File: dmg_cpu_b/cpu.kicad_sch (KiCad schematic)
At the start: 1 part

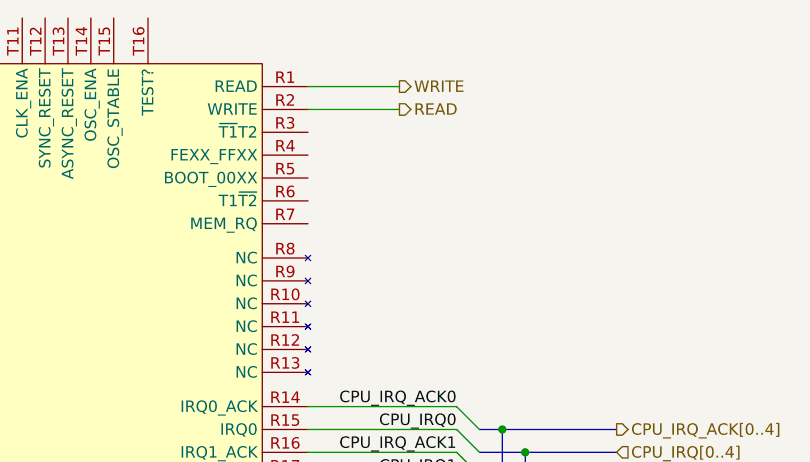
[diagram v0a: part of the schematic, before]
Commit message: addr and data buses added and split on 2 sheets.
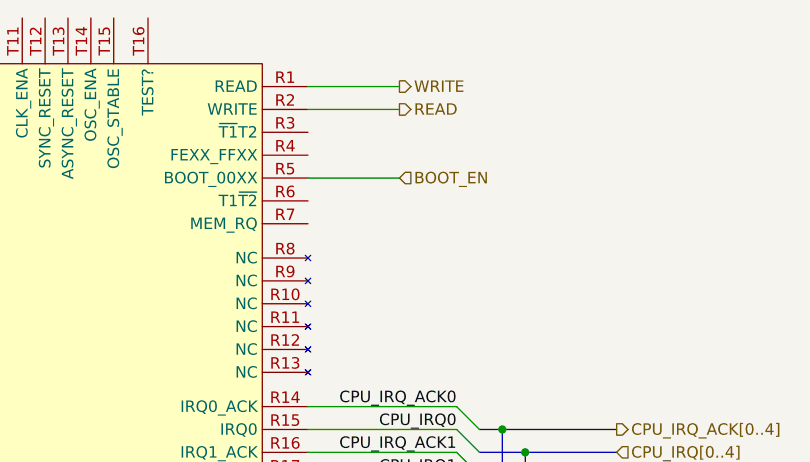
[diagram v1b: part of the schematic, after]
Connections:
- net BOOT_EN: now reaches U?.R5 (BOOT_00XX)
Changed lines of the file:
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@@
+    (stroke (width 0) (type default) (color 0 0 0 0))
+  )
+  (wire (pts (xy 184.15 64.77) (xy 173.99 64.77))
     (stroke (width 0) (type default) (color 0 0 0 0))
   )
@@
     (effects (font (size 1.27 1.27)) (justify right bottom))
   )
+  (hierarchical_label "BOOT_EN" (shape input) (at 184.15 64.77 0)
+    (effects (font (size 1.27 1.27)) (justify left))
+  )
   (hierarchical_label "CPU_IRQ[0..4]" (shape output) (at 363.855 252.73 0)

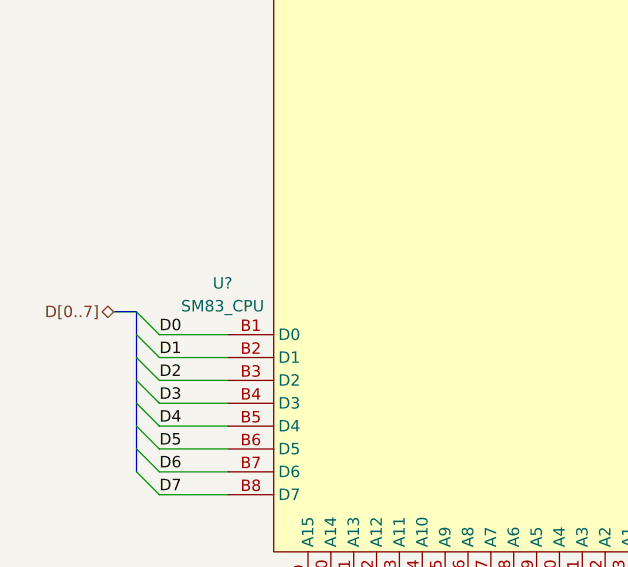
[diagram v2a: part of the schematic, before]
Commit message: fixes made following review
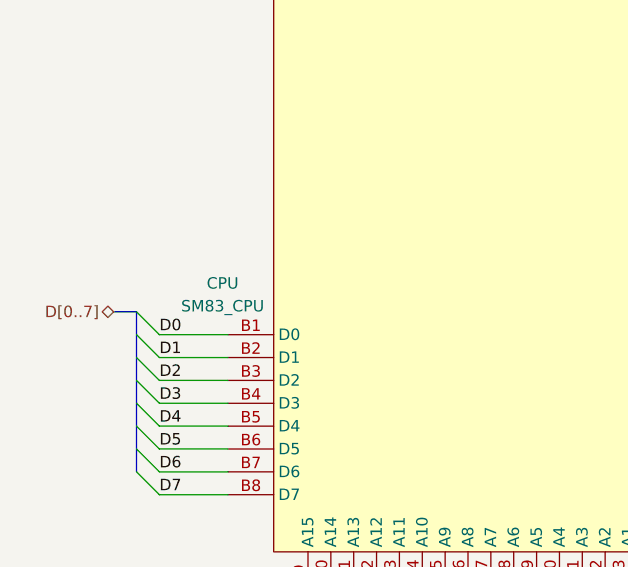
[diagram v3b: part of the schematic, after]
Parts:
- gave numbers to parts that had none: 1
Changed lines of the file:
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@@
   (symbol (lib_id "DMG_CPU_Cells:SM83_CPU") (at 139.7 91.44 0) (unit 1)
     (in_bom yes) (on_board yes) (fields_autoplaced)
-    (property "Reference" "U?" (id 0) (at 104.8166 100.9735 0))
+    (property "Reference" "CPU" (id 0) (at 104.8166 100.9735 0))
     (property "Value" "SM83_CPU" (id 1) (at 104.8166 103.5104 0))
     (property "Footprint" "" (id 2) (at 143.51 91.44 0)

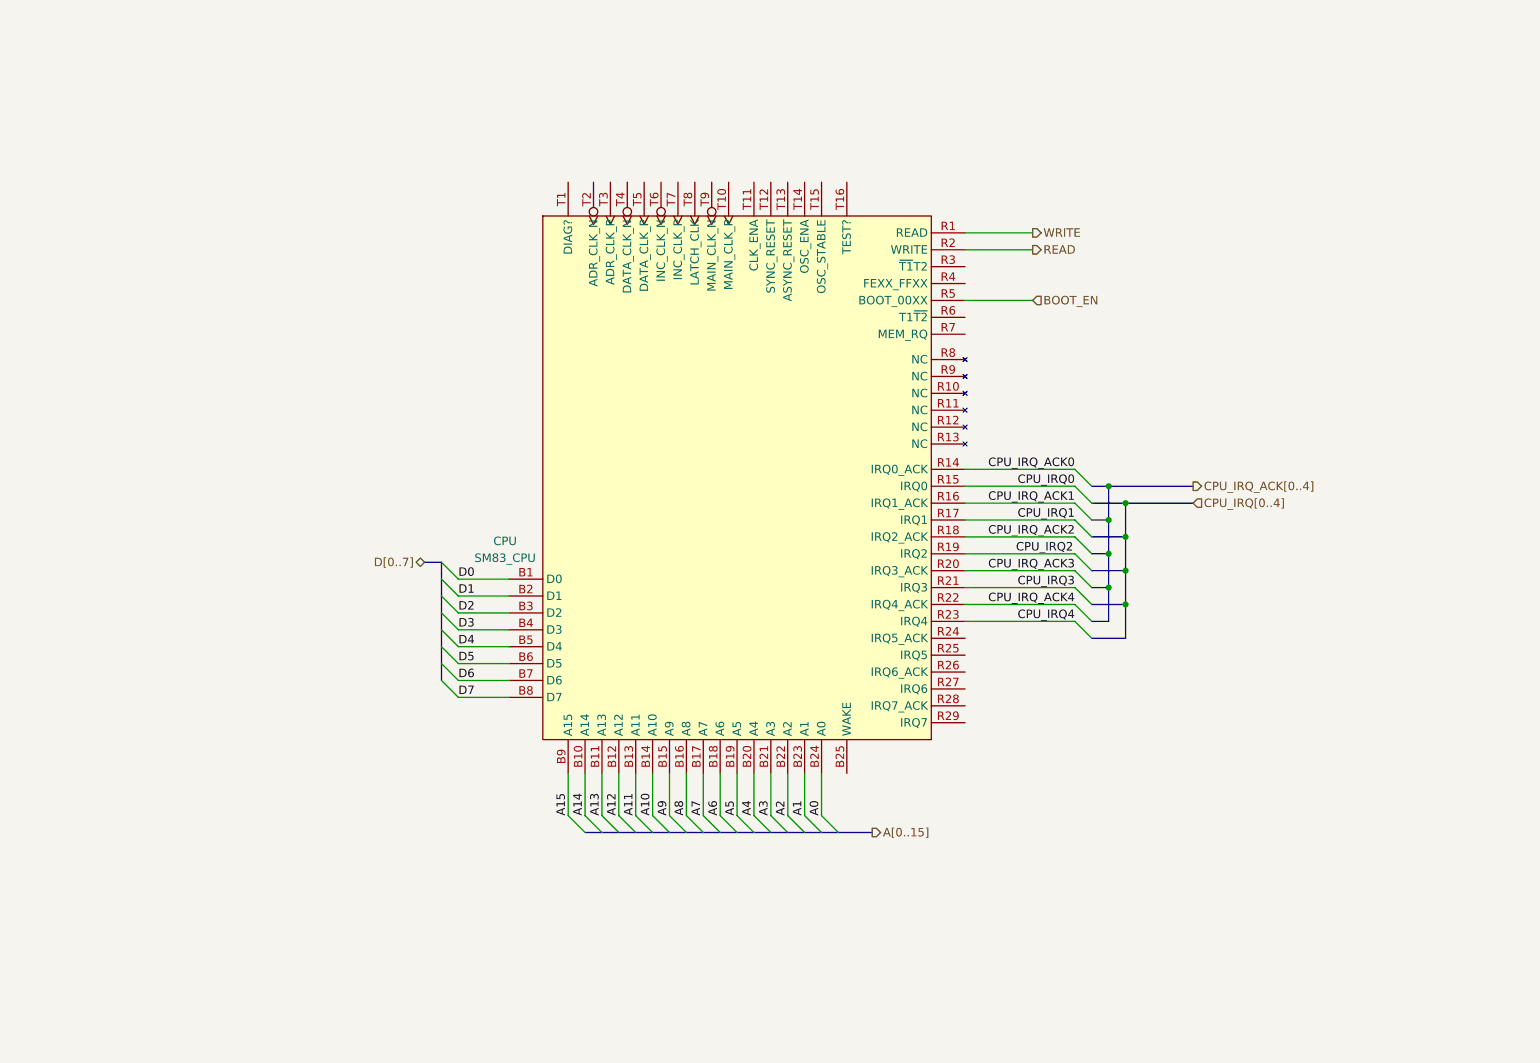
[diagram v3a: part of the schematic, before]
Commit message: VRAM interface sheet added but various edits in existing sheets. Notable merge of RESET, CLOCKS and FF04 DIV sheets
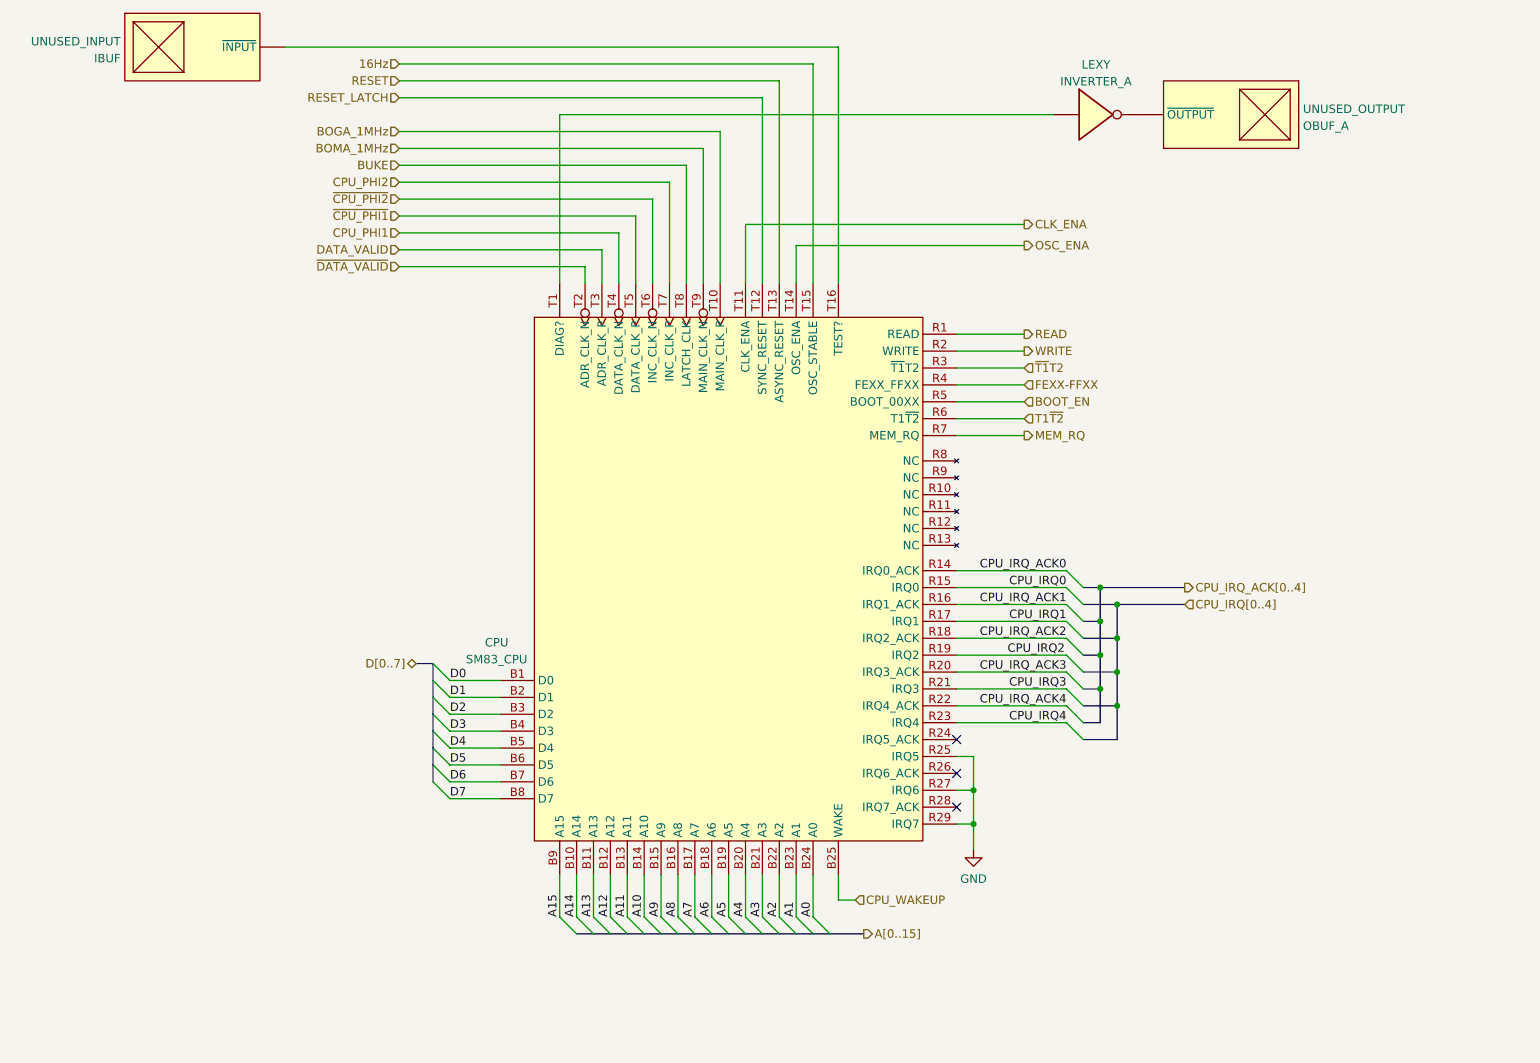
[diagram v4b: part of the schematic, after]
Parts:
- added LEXY: INVERTER_A, symbol DMG_CPU_Cells:INVERTER_A
- added UNUSED_INPUT: IBUF, symbol DMG_CPU_Cells:IBUF
- added UNUSED_OUTPUT: OBUF_A, symbol DMG_CPU_Cells:OBUF_A
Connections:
- net READ: now also CPU.R1 (READ); no longer CPU.R2 (WRITE)
- net WRITE: now also CPU.R2 (WRITE); no longer CPU.R1 (READ)
- net CPU_WAKEUP: now reaches CPU.B25 (WAKE)
- net GND: now reaches CPU.R25 (IRQ5)
- net GND: now also CPU.R27 (IRQ6), CPU.R29 (IRQ7)
- net ~{T1}T2: now reaches CPU.R3 (~{T1}T2)
- net FEXX-FFXX: now reaches CPU.R4 (FEXX_FFXX)
- net T1~{T2}: now reaches CPU.R6 (T1~{T2})
- net MEM_RQ: now reaches CPU.R7 (MEM_RQ)
- net at CPU.T1 (DIAG?): now also LEXY.1
- net BOGA_1MHz: now reaches CPU.T10 (MAIN_CLK_P)
- net CLK_ENA: now reaches CPU.T11 (CLK_ENA)
- net RESET_LATCH: now reaches CPU.T12 (SYNC_RESET)
- net RESET: now reaches CPU.T13 (ASYNC_RESET)
- net OSC_ENA: now reaches CPU.T14 (OSC_ENA)
- net 16Hz: now reaches CPU.T15 (OSC_STABLE)
- net at CPU.T16 (TEST?): now also UNUSED_INPUT.1 (~{INPUT})
- net ~{DATA_VALID}: now reaches CPU.T2 (ADR_CLK_N)
- net DATA_VALID: now reaches CPU.T3 (ADR_CLK_P)
- net CPU_PHI1: now reaches CPU.T4 (DATA_CLK_N)
- net ~{CPU_PHI1}: now reaches CPU.T5 (DATA_CLK_P)
- net ~{CPU_PHI2}: now reaches CPU.T6 (INC_CLK_N)
- net CPU_PHI2: now reaches CPU.T7 (INC_CLK_P)
- net BUKE: now reaches CPU.T8 (LATCH_CLK)
- net BOMA_1MHz: now reaches CPU.T9 (MAIN_CLK_N)
- new net: LEXY.2, UNUSED_OUTPUT.1 (~{OUTPUT})
- no-connect marks 0 -> 3
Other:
- moved on the sheet: CPU

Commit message: Minor tweaks to help with clarity.
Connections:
- net T1~{T2}: now also CPU.R3 (~{T1}T2); no longer CPU.R6 (T1~{T2})
- net ~{T1}T2: now also CPU.R6 (T1~{T2}); no longer CPU.R3 (~{T1}T2)
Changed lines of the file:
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@@
     (effects (font (size 1.27 1.27)) (justify right))
   )
-  (hierarchical_label "~{T1}T2" (shape input) (at 182.88 74.93 0)
+  (hierarchical_label "T1~{T2}" (shape input) (at 182.88 74.93 0)
     (effects (font (size 1.27 1.27)) (justify left))
   )
@@
     (effects (font (size 1.27 1.27)) (justify left))
   )
-  (hierarchical_label "T1~{T2}" (shape input) (at 182.88 82.55 0)
+  (hierarchical_label "~{T1}T2" (shape input) (at 182.88 82.55 0)
     (effects (font (size 1.27 1.27)) (justify left))
   )

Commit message: Changes made on review.
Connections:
- net 16Hz renamed RESET_RELEASE
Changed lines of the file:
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@@
-    (effects (font (size 1.27 1.27)) (justify right))
-  )
-  (hierarchical_label "16Hz" (shape input) (at 88.9 29.21 180)
     (effects (font (size 1.27 1.27)) (justify right))
   )
@@
     (effects (font (size 1.27 1.27)) (justify right))
   )
+  (hierarchical_label "RESET_RELEASE" (shape input) (at 88.9 29.21 180)
+    (effects (font (size 1.27 1.27)) (justify right))
+  )
